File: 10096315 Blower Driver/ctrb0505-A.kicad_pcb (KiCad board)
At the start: 4 copper layers, 92.5 x 72 mm, 149 parts, among them IC1 L-BC-SO24, IC2 L-BC-SO08, IC3 L-BC-SO08, IC4 L-BC-SO08, IC5 L-BC-SO08, IC6 REG-BC-DPAK, J1 F-COCMS-MOL43650-0212, J11 F-CO-MOL5566-02, J2 F-CO-HE10-2010D, J22 F-CO-MOL7395M09, J3 F-CO-MOL7395M02, J6 F-CO-MOL7395M08, T1 Q-SOT23-IRLML2803, T10 Q-SOT23-IRLML2803, T2 Q-BC-DPAK-GDS, T3 Q-BC-DPAK-GDS, T4 Q-BC-DPAK-GDS, T5 Q-BC-DPAK-GDS, T6 Q-BC-DPAK-GDS, T7 Q-BC-DPAK-GDS, T8 Q-SOT23-IRLML2803, T9 Q-BC-DPAK-GDS

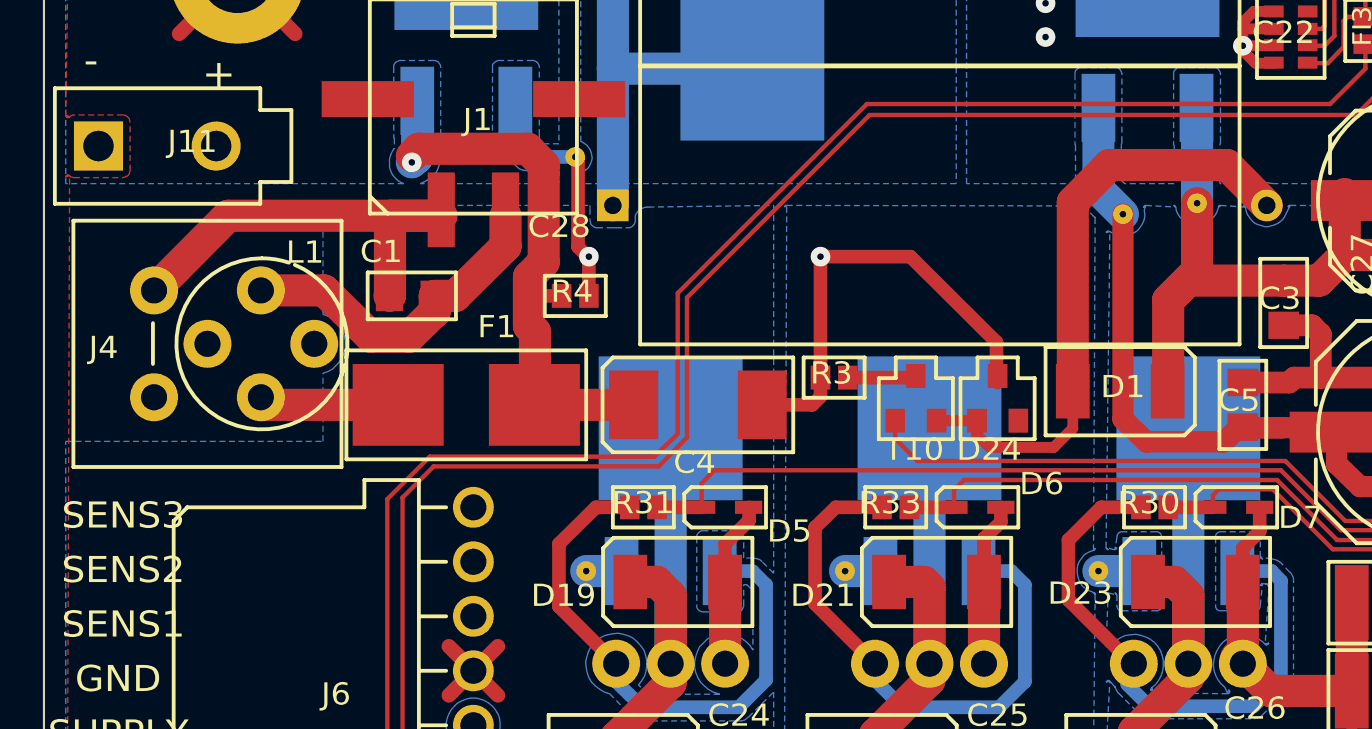
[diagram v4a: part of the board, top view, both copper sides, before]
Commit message: substitute L1 and J4 by real fprints, and add reference to holes
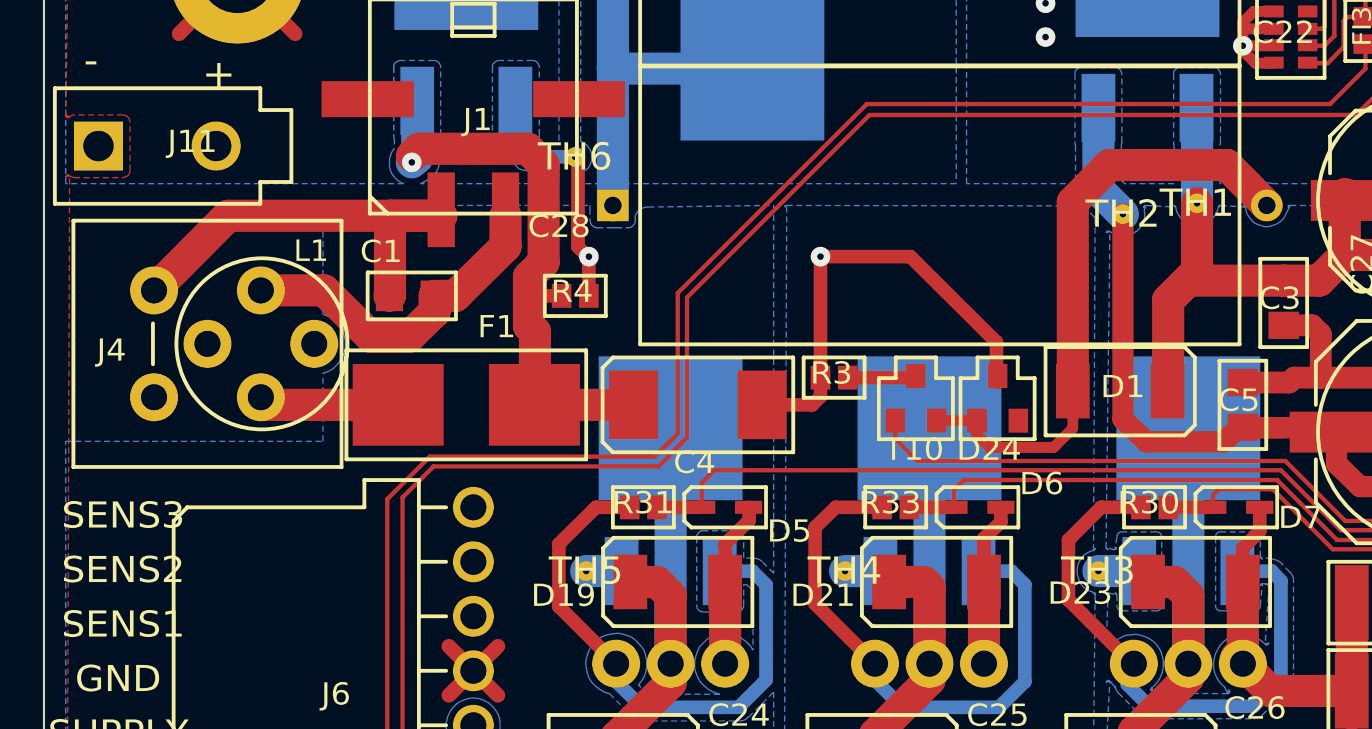
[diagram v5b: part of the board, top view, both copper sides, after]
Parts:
- removed ? (x6): , ctrb0505-A:ThroughHole_36milx12mil_Pad_Cu_Mask
- added J4: JUMPER2_NoCopper, ctrb0505-A:JUMPER2_NoCopper_1, F.Cu at (246.5, 60.6)
- added L1: ELC09DxxxxF_NoCopper, ctrb0505-A:ELC09DxxxxF_NoCopper_1, F.Cu at (251.6, 60.6)
- added TH1: , ctrb0505-A:ThroughHole_36milx12mil_Pad_Cu_Mask, F.Cu at (295.2, 54.0)
- added TH2: , ctrb0505-A:ThroughHole_36milx12mil_Pad_Cu_Mask, F.Cu at (291.7, 54.5)
- added TH3: , ctrb0505-A:ThroughHole_36milx12mil_Pad_Cu_Mask, F.Cu at (290.6, 71.2)
- added TH4: , ctrb0505-A:ThroughHole_36milx12mil_Pad_Cu_Mask, F.Cu at (278.8, 71.2)
- added TH5: , ctrb0505-A:ThroughHole_36milx12mil_Pad_Cu_Mask, F.Cu at (266.7, 71.2)
- added TH6: , ctrb0505-A:ThroughHole_36milx12mil_Pad_Cu_Mask, F.Cu at (266.2, 51.9)
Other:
- board text removed: "J4"
- board text removed: "L1"
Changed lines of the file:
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@@
   (general
     (thickness 1.6)
-    (drawings 76)
+    (drawings 63)
     (tracks 1113)
     (zones 0)
-    (modules 149)
+    (modules 151)
     (nets 71)
   )
@@
     (add_net V-REF-M)
   )
+  (module ctrb0505-A:ELC09DxxxxF_NoCopper_1 (layer F.Cu)
+    (at 251.6046 60.5636)
+    (attr virtual)
+    (fp_text reference L1 (at 2.2938 -4.328) (layer F.SilkS)
+      (effects (font (size 1 1) (thickness 0.15)))
+    )
+    (fp_text value ELC09DxxxxF_NoCopper (at 0 6.3072) (layer F.Fab)
+      (effects (font (size 1 1) (thickness 0.15)))
+    )
+    (fp_circle (center 0 0) (end 0 5.6322) (layer F.CrtYd) (width 0.05))
+    (fp_circle (center 0 0) (end 3.9878 0) (layer F.SilkS) (width 0.1778))
+    (fp_circle (center 0 0) (end 0 3.9878) (layer F.Fab) (width 0.1))
+    (pad 2 smd oval (at 0 2.5) (size 2.2352 2.2352) (layers F.Mask))
+    (pad 1 smd oval (at 0 -2.5) (size 2.2352 2.2352) (layers F.Mask))
+    (model ${KISYS3DMOD}/Inductor_THT.3dshapes/L_Radial_D7.5mm_P5.00mm_Fastron_07P.wrl
+      (offset (xyz 0 2.5 0))
+      (scale (xyz 1 1 1))
+      (rotate (xyz 0 0 90))
+    )
+  )
+  (module ctrb0505-A:JUMPER2_NoCopper_1 (layer F.Cu)
+    (at 246.5246 60.5636)
+    (attr virtual)
+    (fp_text reference J4 (at -1.9304 0.3048 unlocked) (layer F.SilkS)
+      (effects (font (size 1.033069 1.086612) (thickness 0.127)))
+    )
+    (fp_text value JUMPER2_NoCopper (at 7.62 -1.016 unlocked) (layer F.SilkS) hide
+      (effects (font (size 1.332992 1.40208) (thickness 0.254)))
+    )
+    (fp_line (start 0 -0.9525) (end 0 0.9525) (layer F.SilkS) (width 0.1778))
+    (pad 1 smd circle (at 0 -2.4892) (size 2.2352 2.2352) (layers F.Mask))
+    (pad 2 smd circle (at 0 2.4892) (size 2.2352 2.2352) (layers F.Mask))
+  )
   (module ctrb0505-A:FEE_COMP_1 (layer F.Cu)
     (at 315.1046 105.6486)
@@
   (module ctrb0505-A:ThroughHole_36milx12mil_Pad_Cu_Mask (layer F.Cu)
     (at 295.191 54.0104)
-    (fp_text reference "" (at 0 0) (layer F.SilkS)
+    (fp_text reference TH1 (at 0 0) (layer F.SilkS)
       (effects (font (size 1.27 1.27) (thickness 0.15)))
     )
@@
   (module ctrb0505-A:ThroughHole_36milx12mil_Pad_Cu_Mask (layer F.Cu)
     (at 291.7366 54.5184)
-    (fp_text reference "" (at 0 0) (layer F.SilkS)
+    (fp_text reference TH2 (at 0 0) (layer F.SilkS)
       (effects (font (size 1.27 1.27) (thickness 0.15)))
     )
@@
   (module ctrb0505-A:ThroughHole_36milx12mil_Pad_Cu_Mask (layer F.Cu)
     (at 290.5936 71.1554)
-    (fp_text reference "" (at 0 0) (layer F.SilkS)
+    (fp_text reference TH3 (at 0 0) (layer F.SilkS)
       (effects (font (size 1.27 1.27) (thickness 0.15)))
     )
@@
   (module ctrb0505-A:ThroughHole_36milx12mil_Pad_Cu_Mask (layer F.Cu)
     (at 278.7826 71.1554)
-    (fp_text reference "" (at 0 0) (layer F.SilkS)
+    (fp_text reference TH4 (at 0 0) (layer F.SilkS)
       (effects (font (size 1.27 1.27) (thickness 0.15)))
     )
@@
   (module ctrb0505-A:ThroughHole_36milx12mil_Pad_Cu_Mask (layer F.Cu)
     (at 266.7176 71.1554)
-    (fp_text reference "" (at 0 0) (layer F.SilkS)
+    (fp_text reference TH5 (at 0 0) (layer F.SilkS)
       (effects (font (size 1.27 1.27) (thickness 0.15)))
     )
@@
   (module ctrb0505-A:ThroughHole_36milx12mil_Pad_Cu_Mask (layer F.Cu)
     (at 266.2096 51.8514)
-    (fp_text reference "" (at 0 0) (layer F.SilkS)
+    (fp_text reference TH6 (at 0 0) (layer F.SilkS)
       (effects (font (size 1.27 1.27) (thickness 0.15)))
     )
@@
   (gr_line (start 241.4446 34.6048) (end 333.9514 34.6048) (layer B.Mask) (width 0.9906))
   (gr_line (start 241.4446 106.5884) (end 241.4446 34.6048) (layer B.Mask) (width 0.9906))
-  (gr_arc (start 251.6046 60.5636) (end 251.6046 56.5758) (angle -255.6) (layer F.SilkS) (width 0.1778))
-  (gr_arc (start 251.6046 60.5636) (end 255.538852 61.214911) (angle -76.8) (layer F.SilkS) (width 0.1778))
-  (gr_arc (start 251.6046 60.5636) (end 252.863345 56.779672) (angle -18.4) (layer F.SilkS) (width 0.1778))
-  (gr_line (start 246.5246 61.5034) (end 246.5246 59.5984) (layer F.SilkS) (width 0.1778))
-  (gr_text J4 (at 243.5274 61.351) (layer F.SilkS)
-    (effects (font (size 1.033069 1.086612) (thickness 0.127)) (justify left bottom))
-  )
-  (gr_text L1 (at 252.7222 56.906) (layer F.SilkS)
-    (effects (font (size 1.033069 1.086612) (thickness 0.127)) (justify left bottom))
-  )
   (gr_text "10096505 " (at 283.253 150.505) (layer F.SilkS)
     (effects (font (size 1.73289 1.822704) (thickness 0.0762)) (justify left bottom))
@@
     (effects (font (size 1.73289 1.822704) (thickness 0.0762)) (justify left bottom mirror))
   )
-  (gr_circle (center 251.6046 60.5636) (end 255.5924 60.5636) (layer F.Fab) (width 0.0762))
-  (gr_arc (start 246.5246 63.1036) (end 246.2198 63.1036) (angle -180) (layer F.Fab) (width 0.0762))
-  (gr_arc (start 246.5246 58.0236) (end 246.8294 58.0236) (angle -180) (layer F.Fab) (width 0.0762))
-  (gr_line (start 246.8548 63.1036) (end 246.8548 58.0236) (layer F.Fab) (width 0.0762))
-  (gr_line (start 246.2198 63.1036) (end 246.2198 58.0236) (layer F.Fab) (width 0.0762))
-  (gr_text L1 (at 250.9188 60.9192) (layer F.Fab)
-    (effects (font (size 0.866445 0.911352) (thickness 0.0254)) (justify left bottom))
-  )
-  (gr_text J4 (at 244.264 60.9192) (layer F.Fab)
-    (effects (font (size 0.866445 0.911352) (thickness 0.0254)) (justify left bottom))
-  )
   (gr_line (start 355.4652 75.6004) (end 355.9478 74.1018) (layer B.Fab) (width 0.0762))
